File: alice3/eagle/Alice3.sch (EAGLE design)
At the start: 14 parts, among them IC1 27C512, IC2 128k x 8 RAM, IC3 Z80, IC4 GAL22V10, IC5 i8259

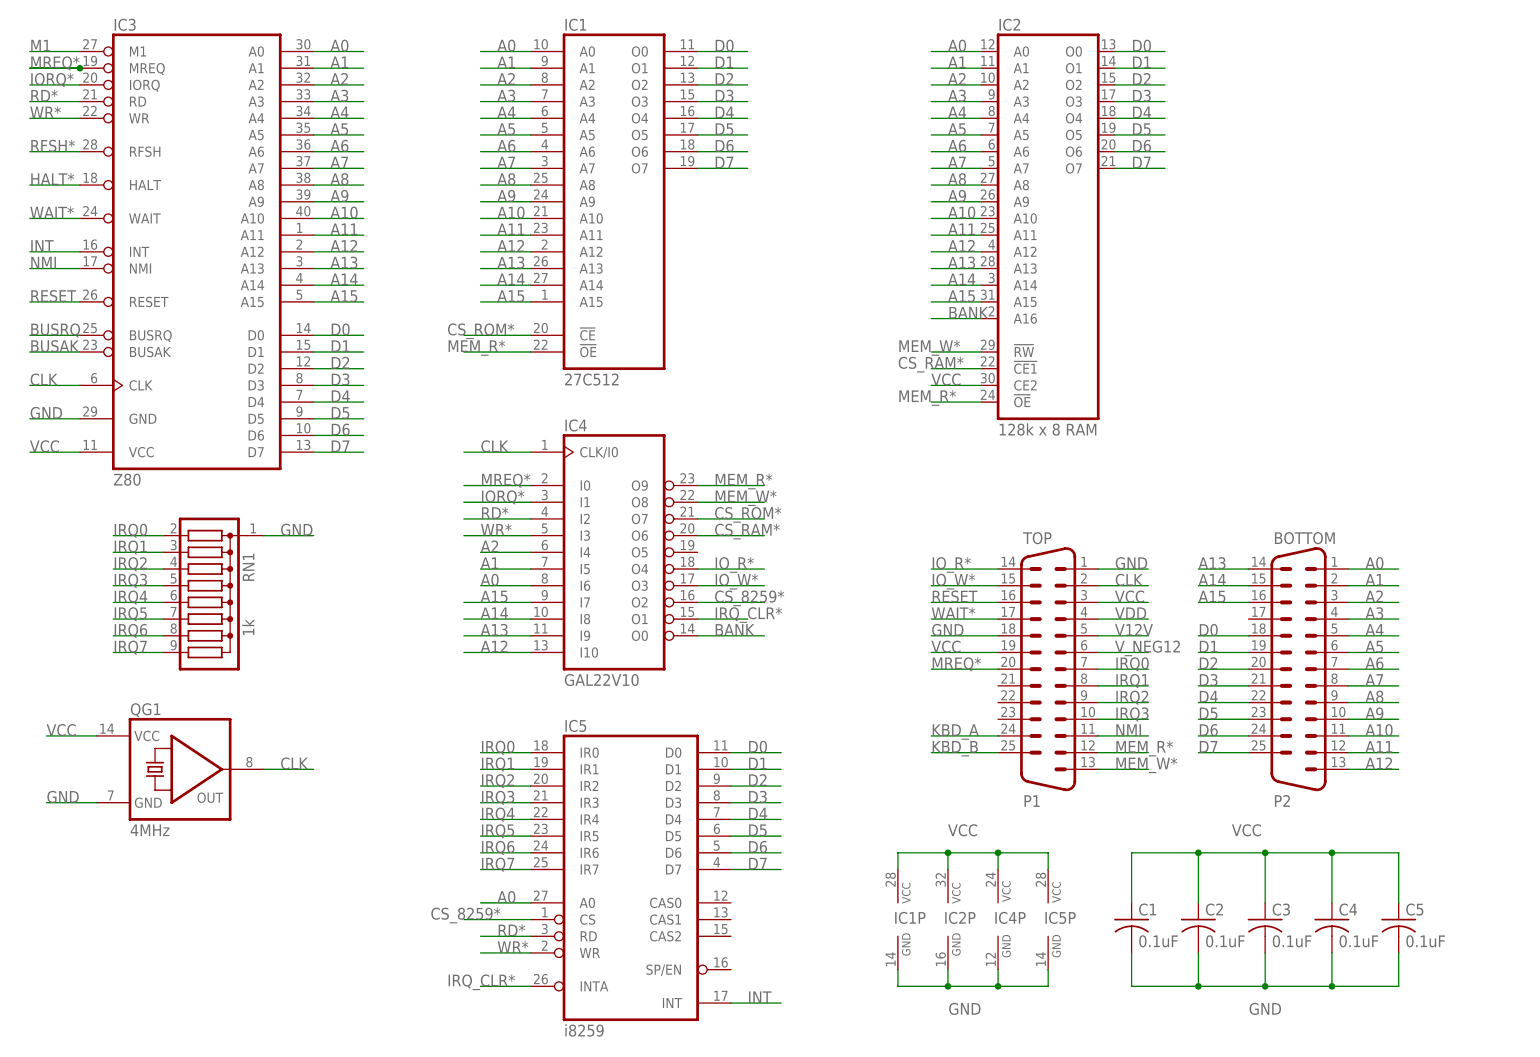
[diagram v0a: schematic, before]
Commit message: New version - Added '*' to active-low signal names (e.g. RESET*) - Connected RESET* and M1 to GAL - More decoupling caps! - Moved some components around on PCB - Remove unused .pro file
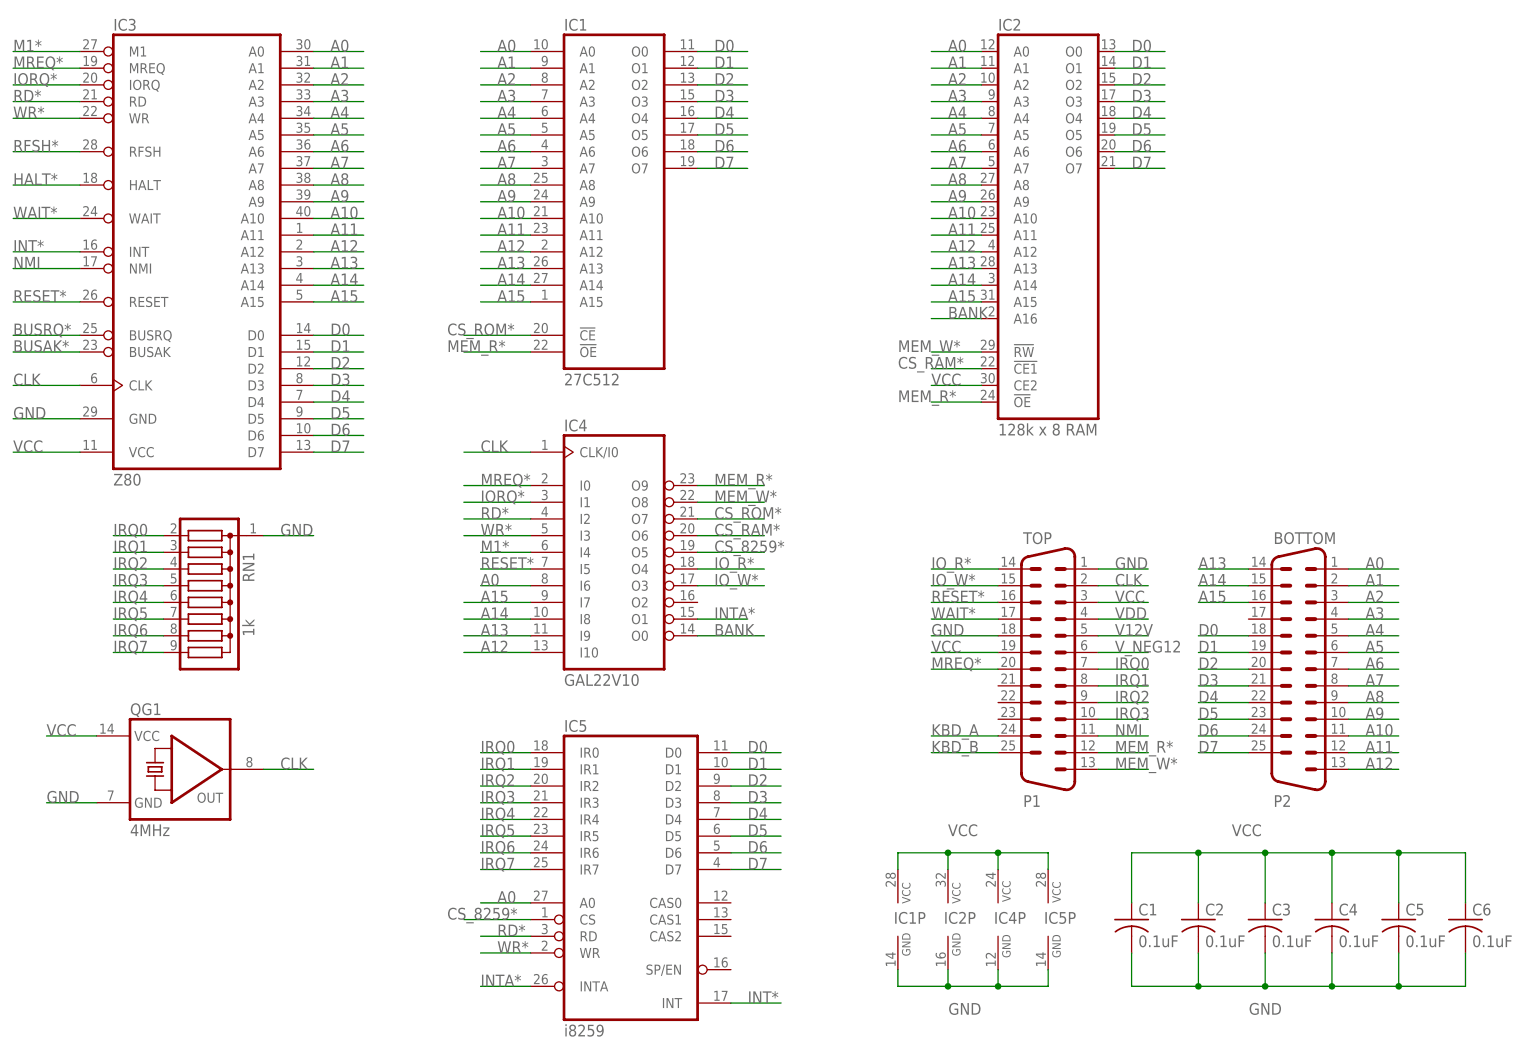
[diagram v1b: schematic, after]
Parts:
- added C6: 0.1uF, resistor:C-USC1206
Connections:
- net BUSAK renamed BUSAK*
- net BUSRQ renamed BUSRQ*
- net INT renamed INT*
- net IRQ_CLR* renamed INTA*
- removed net M1: IC3.M1
- removed net RESET: IC3.RESET, TOP.16
- new net M1*: IC3.M1, IC4G$1.I4
- new net RESET*: IC3.RESET, IC4G$1.I5, TOP.16
- net A1: no longer IC4G$1.I5
- net A2: no longer IC4G$1.I4
- net CS_8259*: now also IC4G$1.O5; no longer IC4G$1.O2
- net GND: now also C6.2
- net VCC: now also C6.1
